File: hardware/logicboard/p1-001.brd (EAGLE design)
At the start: 91 x 57 mm, 36 parts, among them J0 DC9V, J4A RLYOUT-A, J4B RLYOUT-B, J4C RLYOUT-C, J7 DIN5, K1A G5V1, K1B G5V1, K1C G5V1, T1A 2SC1815, T1B 2SC1815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

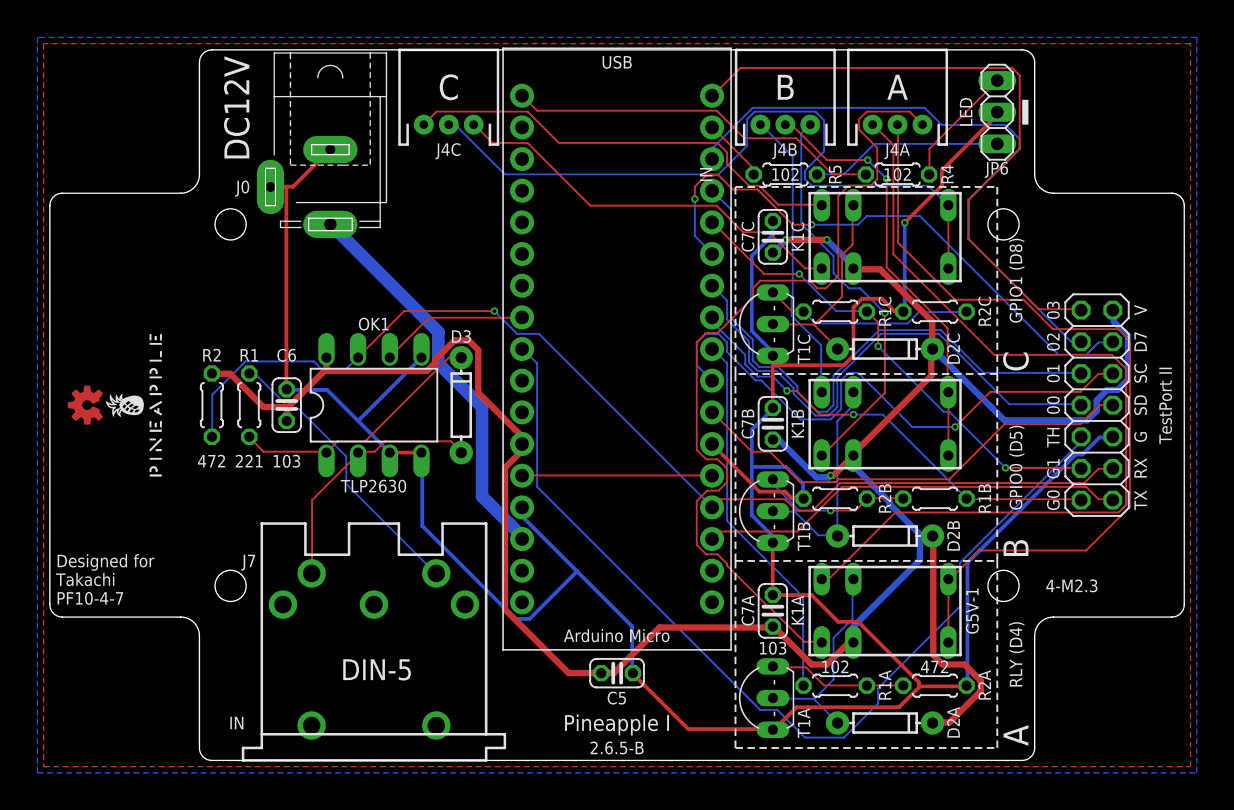
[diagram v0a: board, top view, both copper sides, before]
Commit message: J1, J5, and J20.
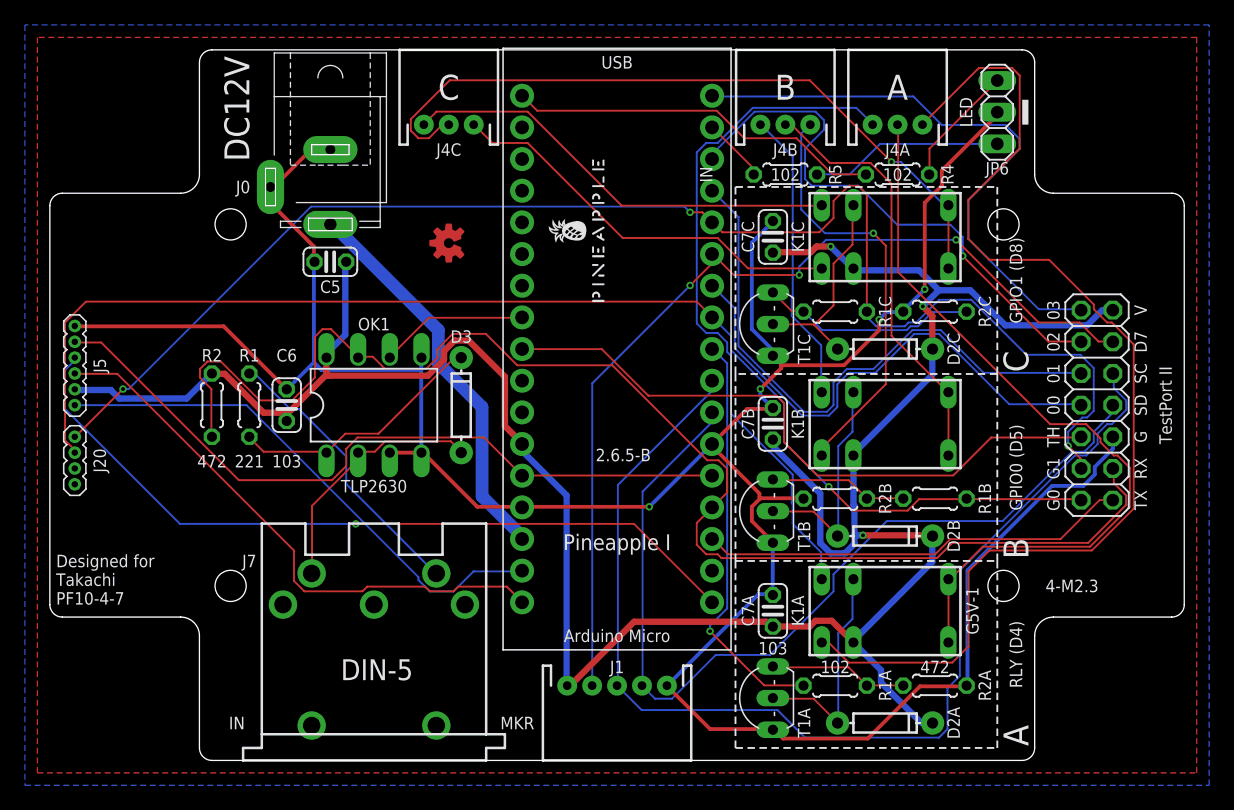
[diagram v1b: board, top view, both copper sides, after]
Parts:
- added J1: (no value), SparkFun-Connectors:JST-5-PTH
- added J20: (no value), SparkFun-Connectors:1X04_1.27MM
- added J5: (no value), SparkFun-Connectors:1X06_1.27MM
- moved C5 40.2 mm to (22.5, 40.0), turned to 180 degrees
- moved U$1 38.2 mm to (44.5, 42.5)
- moved LOGO1 31.8 mm to (32.0, 41.5)
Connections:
- net D7GATE: now also J1.4
- net GND: now also J1.1, J5.6
- net GPIO0: now also J20.3
- net GPIO1: now also J20.4
- net MISO: now also J5.1
- net MOSI: now also J5.4
- net RST: now also J5.5
- net SCK: now also J5.3
- net SCL: now also J1.3
- net SDA: now also J1.2
- net VCC: now also J1.5, J5.2
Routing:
- net GPIO1: track 38.9 -> 115.8 mm
- net GPIO0: track 36.4 -> 102.9 mm, vias 2 -> 1
- net MOSI: track 0.00 -> 62.8 mm, vias 0 -> 1
- net SCK: track 0.00 -> 45.6 mm
- net SCL: track 47.0 -> 91.8 mm, vias 1 -> 0
- net RST: track 15.3 -> 59.2 mm
- net MISO: track 0.00 -> 42.9 mm
- net SDA: track 37.0 -> 73.9 mm
- net D7GATE: track 46.9 -> 76.7 mm, vias 2 -> 3
- net THS: track 76.5 -> 52.2 mm
- net RX: track 87.5 -> 108.6 mm, vias 1 -> 0
- net RLYOUT3: track 68.5 -> 89.3 mm
- net RLYOUT1: track 71.4 -> 55.2 mm
- net VCC: track 188.0 -> 199.6 mm
- net GND: track 235.7 -> 228.8 mm, vias 1 -> 4
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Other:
- board text added: "MKR"

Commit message: Silk.
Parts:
- moved U$1 36.3 mm to (11.0, 28.5)
- moved LOGO1 30.0 mm to (5.00, 28.5)
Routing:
- net D7GATE: track 76.7 -> 112.7 mm, vias 3 -> 1
- net RLYOUT3: track 89.3 -> 54.8 mm, vias 0 -> 1
- net VCC: track 199.6 -> 231.1 mm
- net GND: track 228.8 -> 246.7 mm, vias 4 -> 2
- net DTCT1: track 48.2 -> 38.8 mm, vias 0 -> 1
- net MOSI: track 62.8 -> 72.2 mm, vias 1 -> 0
- net RX: track 108.6 -> 102.1 mm, vias 0 -> 1
- net SDA: track 73.9 -> 80.3 mm
- net GPIO1: track 115.8 -> 122.0 mm, vias 3 -> 1
- net DTCT2: track 44.9 -> 50.4 mm, vias 1 -> 0
- net RLYOUT1: track 55.2 -> 59.6 mm
- net RLY: track 33.0 -> 30.1 mm, vias 1 -> 0
- net RLYOUT2C: track 58.3 -> 55.7 mm, vias 1 -> 0
- net RLYOUT3B: track 34.1 -> 31.8 mm, vias 1 -> 0
- net SCL: track 91.8 -> 90.6 mm, vias 0 -> 1
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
